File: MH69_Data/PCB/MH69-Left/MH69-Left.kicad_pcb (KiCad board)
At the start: 2 copper layers, 163.2 x 92 mm, 85 parts, among them U1 nice_nano

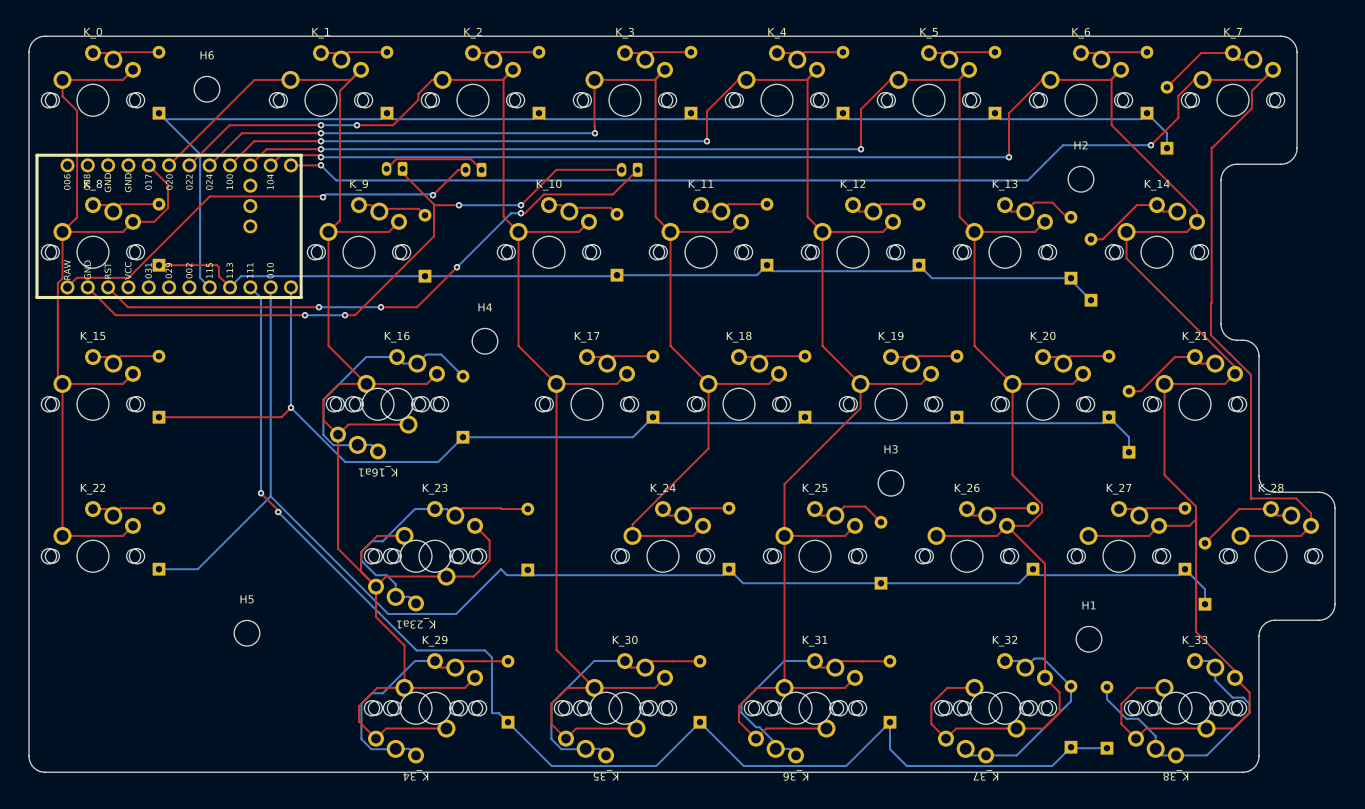
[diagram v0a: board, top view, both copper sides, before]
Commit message: Added Kailh Plated 1Us to Left
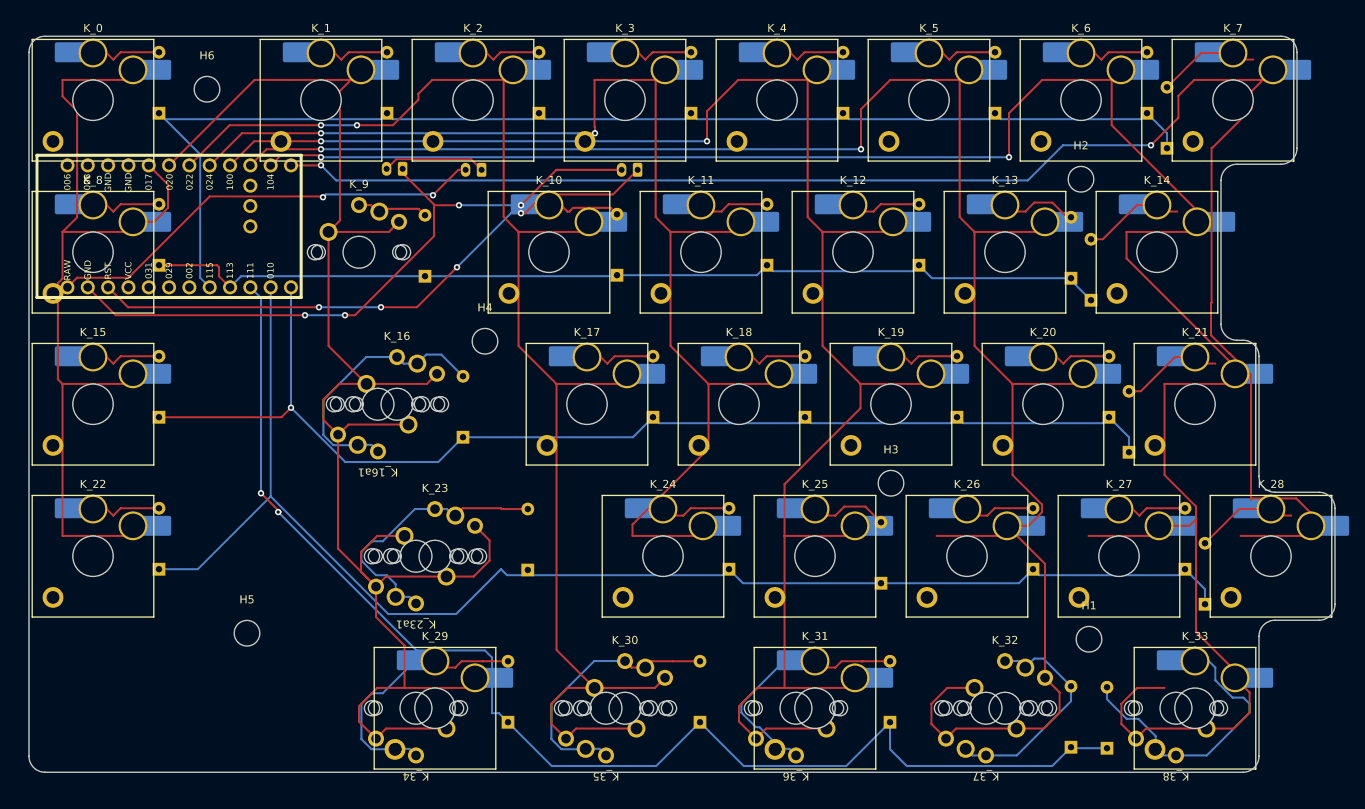
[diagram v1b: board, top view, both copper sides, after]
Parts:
- K_0, K_1, K_10, K_11, K_12, K_13, K_14, K_15, K_17, K_18, K_19, K_2, K_20, K_21, K_22, K_24, K_25, K_26, K_27, K_28, K_29, K_3, K_31, K_33, K_4, K_5, K_6, K_7, K_8: footprint cb:Choc-MX-19mm-1u -> PCM_Switch_Keyboard_Hotswap_Kailh:SW_Hotswap_Kailh_Choc_V2_Plated_1.00u

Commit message: some kicad work
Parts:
- removed K_16a1: KEYSW, cb:Choc-MX-19mm-1.75u
- K_0, K_1, K_10, K_11, K_12, K_13, K_14, K_15, K_17, K_18, K_19, K_2, K_20, K_21, K_22, K_24, K_25, K_26, K_27, K_28, K_29, K_3, K_31, K_33, K_4, K_5, K_6, K_7, K_8: footprint PCM_Switch_Keyboard_Hotswap_Kailh:SW_Hotswap_Kailh_Choc_V2_Plated_1.00u -> PCM_Switch_Keyboard_Hotswap_Kailh:SW_Hotswap_Kailh_Choc_V1_Plated_1.00u
- K_16, K_23, K_30, K_32, K_9: footprint cb:Choc-MX-19mm-1.5u -> PCM_Switch_Keyboard_Hotswap_Kailh:SW_Hotswap_Kailh_Choc_V1_Plated_1.50u
- moved K_21 7.35 mm to (170.8, 99.8)
- moved K_20 6.35 mm to (152.8, 99.8)
- moved K_22 6.18 mm to (41.8, 124.8)
- moved K_19 5.35 mm to (134.8, 99.8)
- moved K_18 4.35 mm to (116.8, 99.8)
- moved K_15 4.26 mm to (41.8, 103.8)
- moved K_17 3.35 mm to (98.8, 99.8)
- moved K_7 3.10 mm to (179.8, 61.8), turned to 180 degrees
- moved K_9 2.66 mm to (76.3, 80.8)
- moved K_14 2.60 mm to (170.8, 80.8)
- moved K_6 2.60 mm to (161.3, 61.8), turned to 180 degrees
- moved K_8 2.46 mm to (41.8, 82.8)
- moved K_16 2.10 mm to (76.3, 99.8)
- moved K_5 2.10 mm to (142.8, 61.8), turned to 180 degrees
- moved U1 2.00 mm to (51.2, 79.5)
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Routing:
- net col6: track 267.2 -> 0.00 mm, vias 2 -> 0
- net col5: track 243.8 -> 0.00 mm, vias 2 -> 0
- net col4: track 223.2 -> 0.00 mm, vias 2 -> 0
- net col7: track 209.1 -> 0.00 mm, vias 2 -> 0
- net col1: track 208.5 -> 0.00 mm
- net col2: track 176.9 -> 0.00 mm, vias 2 -> 0
- net row3: track 174.7 -> 0.00 mm
- net row4: track 162.8 -> 0.00 mm, vias 2 -> 0
- net col3: track 159.3 -> 0.00 mm, vias 2 -> 0
- net row0: track 157.0 -> 0.00 mm
- net row2: track 146.7 -> 0.00 mm, vias 1 -> 0
- net row1: track 122.0 -> 0.00 mm
- net col0: track 107.7 -> 0.00 mm
- net Net-(Batt1-Pin_1): track 84.1 -> 0.00 mm, vias 4 -> 0
- net Net-(RST1-A): track 74.3 -> 0.00 mm, vias 4 -> 0
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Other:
- board text added: "MH69-L V0"
- board text removed: "CB70S-L v3"

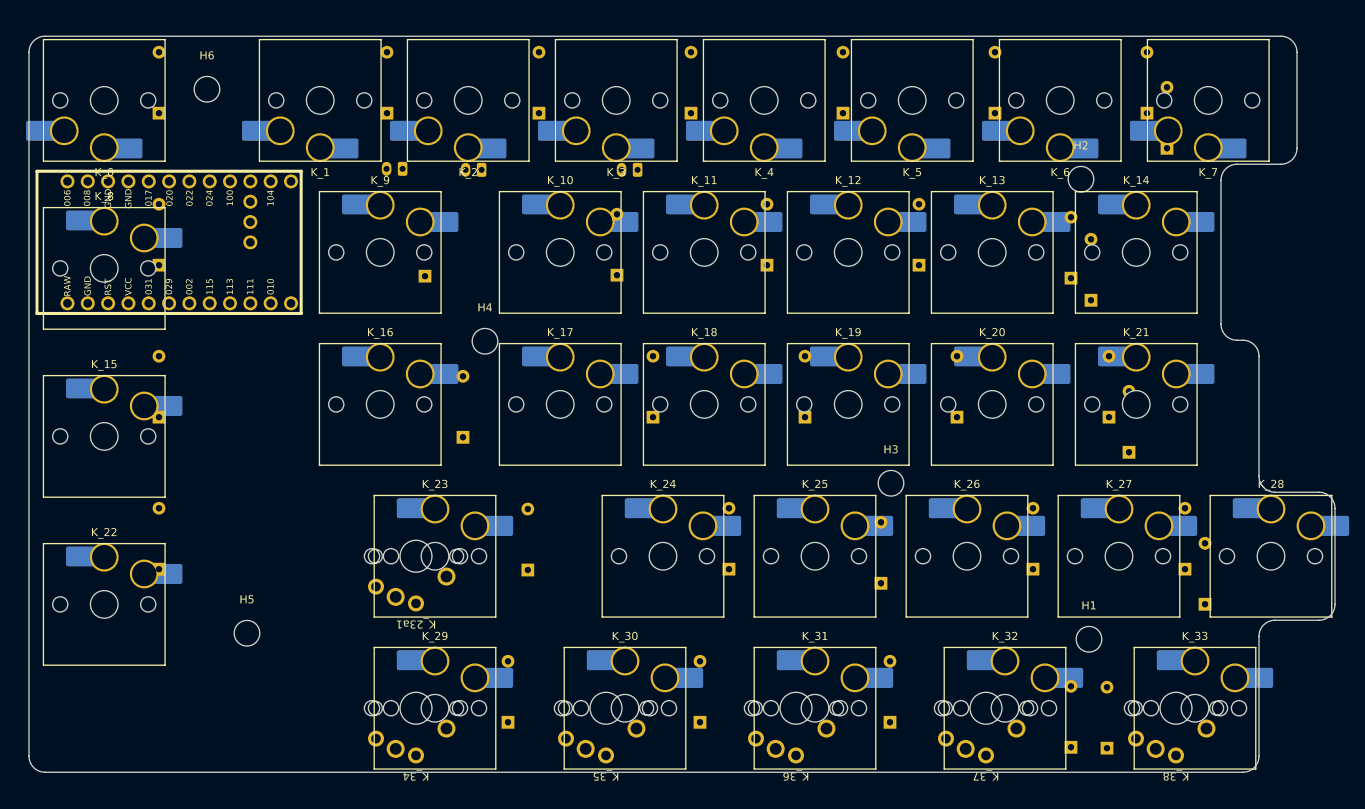
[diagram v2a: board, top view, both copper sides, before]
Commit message: Left side layout progress
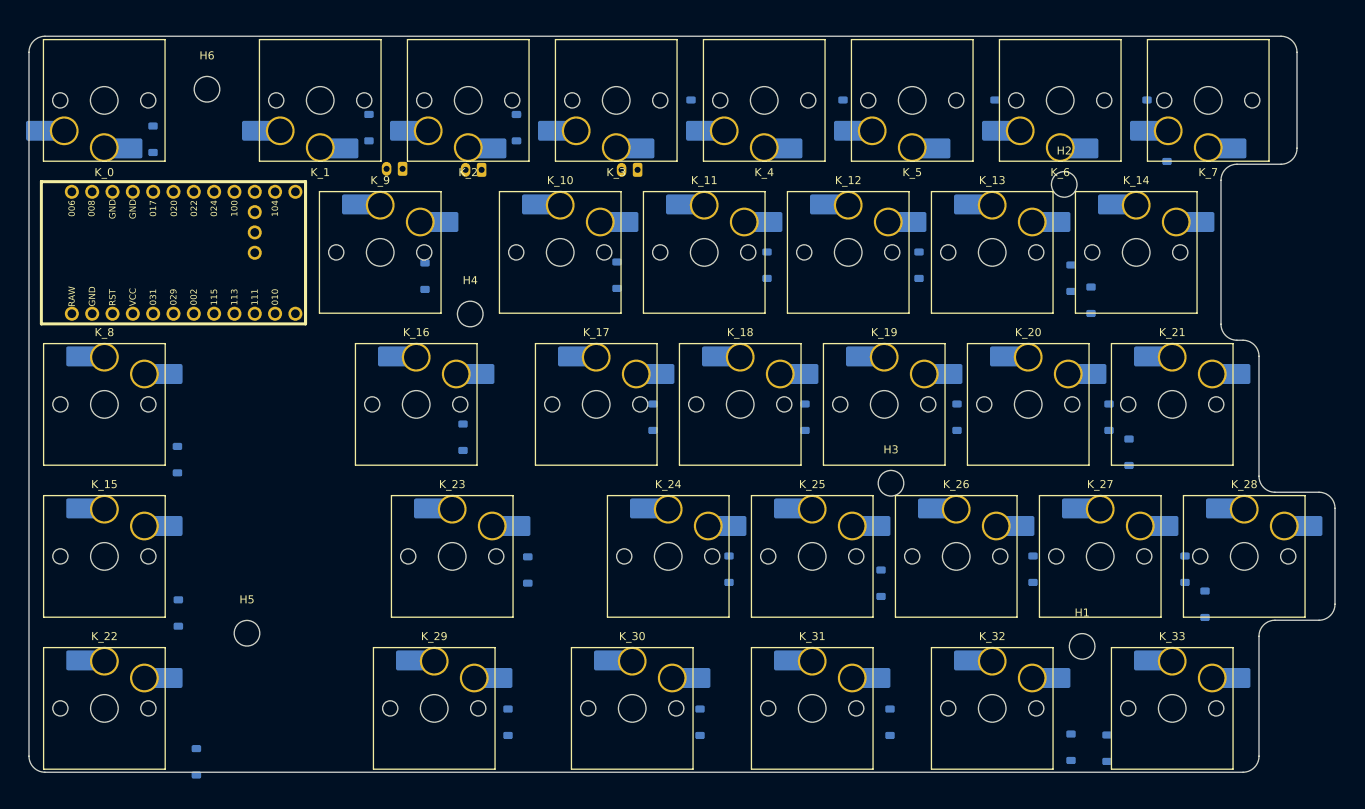
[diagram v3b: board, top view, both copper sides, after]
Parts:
- removed K_23a1: KEYSW, cb:Choc-MX-19mm-2.25u
- removed K_34, K_35, K_36, K_37, K_38: KEYSW, cb:Choc-MX-19mm-1.25u
- D_0, D_1, D_10, D_11, D_12, D_13, D_14, D_15, D_16, D_17, D_18, D_19, D_2, D_20, D_21, D_22, D_23, D_24, D_25, D_26, D_27, D_28, D_29, D_3, D_30, D_31, D_32, D_33, D_4, D_5, D_6, D_7, D_8, D_9: footprint ScottoKeebs_Components:Diode_DO-35 -> Diode_SMD:D_SOD-123
- K_29: footprint PCM_Switch_Keyboard_Hotswap_Kailh:SW_Hotswap_Kailh_Choc_V1_Plated_1.00u -> PCM_Switch_Keyboard_Hotswap_Kailh:SW_Hotswap_Kailh_Choc_V1_Plated_1.25u
- moved D_15 24.6 mm to (51.0, 125.8)
- moved D_22 24.5 mm to (53.3, 144.4)
- moved D_8 24.4 mm to (50.9, 106.7)
- moved K_8 17.0 mm to (41.8, 99.8)
- moved K_15 15.0 mm to (41.8, 118.8)
- moved K_22 13.0 mm to (41.8, 137.8)
- moved K_16 4.50 mm to (80.8, 99.8)
- moved K_17 4.50 mm to (103.3, 99.8)
- moved K_18 4.50 mm to (121.3, 99.8)
- moved K_19 4.50 mm to (139.3, 99.8)
- moved K_20 4.50 mm to (157.3, 99.8)
- moved K_21 4.50 mm to (175.3, 99.8)
- moved H4 3.87 mm to (87.5, 88.5)
- moved D_2 3.35 mm to (93.3, 65.2)
- moved K_28 3.35 mm to (184.3, 118.8)
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
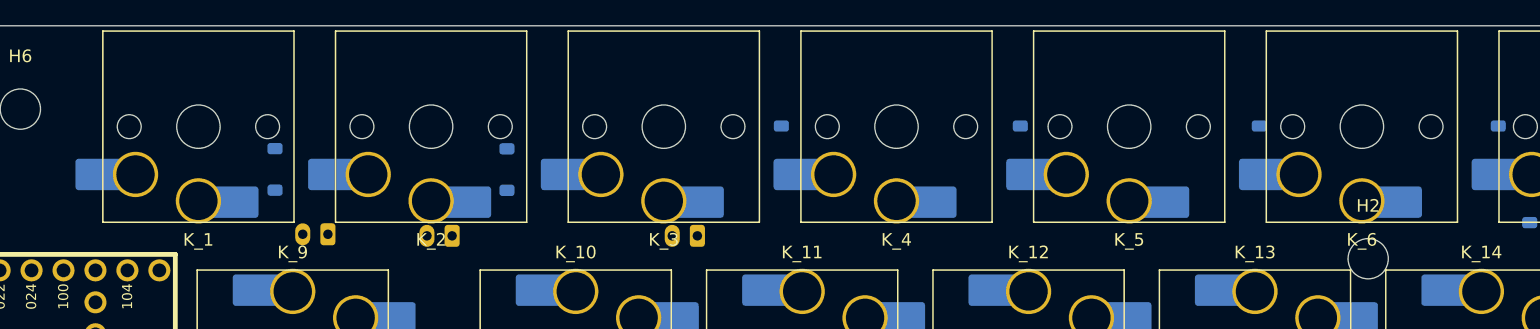
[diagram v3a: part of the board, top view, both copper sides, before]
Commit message: updated left number row
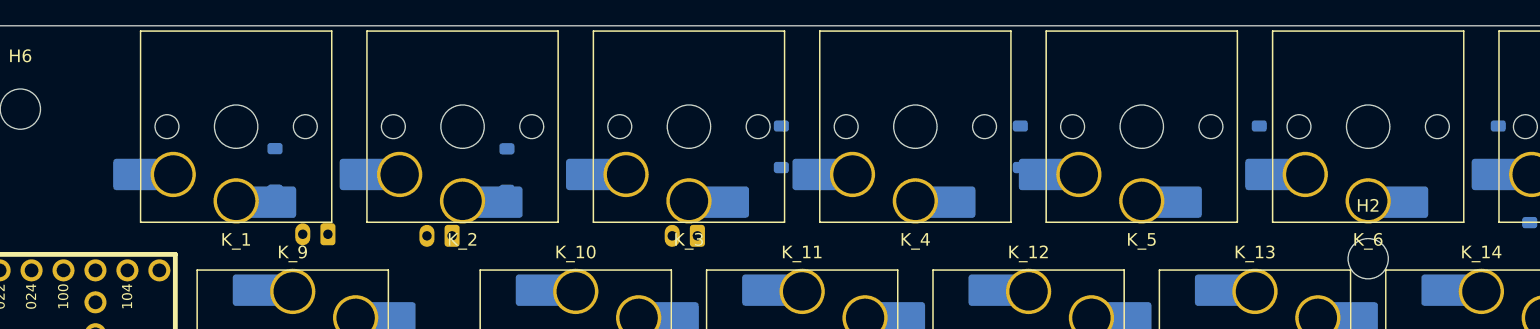
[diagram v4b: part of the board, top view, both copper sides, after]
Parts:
- moved K_1 3.00 mm to (71.8, 61.8)
- moved K_2 2.50 mm to (89.8, 61.8)
- moved K_3 2.00 mm to (107.8, 61.8)
- moved K_4 1.50 mm to (125.8, 61.8)
- moved K_5 1.00 mm to (143.8, 61.8)
- moved K_6 0.50 mm to (161.8, 61.8)
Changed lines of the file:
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@@
 	(footprint "PCM_Switch_Keyboard_Hotswap_Kailh:SW_Hotswap_Kailh_Choc_V1_Plated_1.00u"
 		(layer "F.Cu")
-		(at 105.78 61.77 180)
+		(at 107.78 61.77 180)
 		(descr "Kailh Choc keyswitch V1 CPG1350 V1 Hotswap Plated Keycap 1.00u")
 		(tags "Kailh Choc Keyswitch Switch CPG1350 V1 Hotswap Plated Cutout Keycap 1.00u")
@@
 	(footprint "PCM_Switch_Keyboard_Hotswap_Kailh:SW_Hotswap_Kailh_Choc_V1_Plated_1.00u"
 		(layer "F.Cu")
-		(at 87.28 61.77 180)
+		(at 89.78 61.77 180)
 		(descr "Kailh Choc keyswitch V1 CPG1350 V1 Hotswap Plated Keycap 1.00u")
 		(tags "Kailh Choc Keyswitch Switch CPG1350 V1 Hotswap Plated Cutout Keycap 1.00u")
@@
 	(footprint "PCM_Switch_Keyboard_Hotswap_Kailh:SW_Hotswap_Kailh_Choc_V1_Plated_1.00u"
 		(layer "F.Cu")
-		(at 68.78 61.77 180)
+		(at 71.78 61.77 180)
 		(descr "Kailh Choc keyswitch V1 CPG1350 V1 Hotswap Plated Keycap 1.00u")
 		(tags "Kailh Choc Keyswitch Switch CPG1350 V1 Hotswap Plated Cutout Keycap 1.00u")
@@
 	(footprint "PCM_Switch_Keyboard_Hotswap_Kailh:SW_Hotswap_Kailh_Choc_V1_Plated_1.00u"
 		(layer "F.Cu")
-		(at 161.28 61.77 180)
+		(at 161.78 61.77 180)
 		(descr "Kailh Choc keyswitch V1 CPG1350 V1 Hotswap Plated Keycap 1.00u")
 		(tags "Kailh Choc Keyswitch Switch CPG1350 V1 Hotswap Plated Cutout Keycap 1.00u")
@@
 	(footprint "PCM_Switch_Keyboard_Hotswap_Kailh:SW_Hotswap_Kailh_Choc_V1_Plated_1.00u"
 		(layer "F.Cu")
-		(at 142.78 61.77 180)
+		(at 143.78 61.77 180)
 		(descr "Kailh Choc keyswitch V1 CPG1350 V1 Hotswap Plated Keycap 1.00u")
 		(tags "Kailh Choc Keyswitch Switch CPG1350 V1 Hotswap Plated Cutout Keycap 1.00u")
@@
 	(footprint "PCM_Switch_Keyboard_Hotswap_Kailh:SW_Hotswap_Kailh_Choc_V1_Plated_1.00u"
 		(layer "F.Cu")
-		(at 124.28 61.77 180)
+		(at 125.78 61.77 180)
 		(descr "Kailh Choc keyswitch V1 CPG1350 V1 Hotswap Plated Keycap 1.00u")
 		(tags "Kailh Choc Keyswitch Switch CPG1350 V1 Hotswap Plated Cutout Keycap 1.00u")

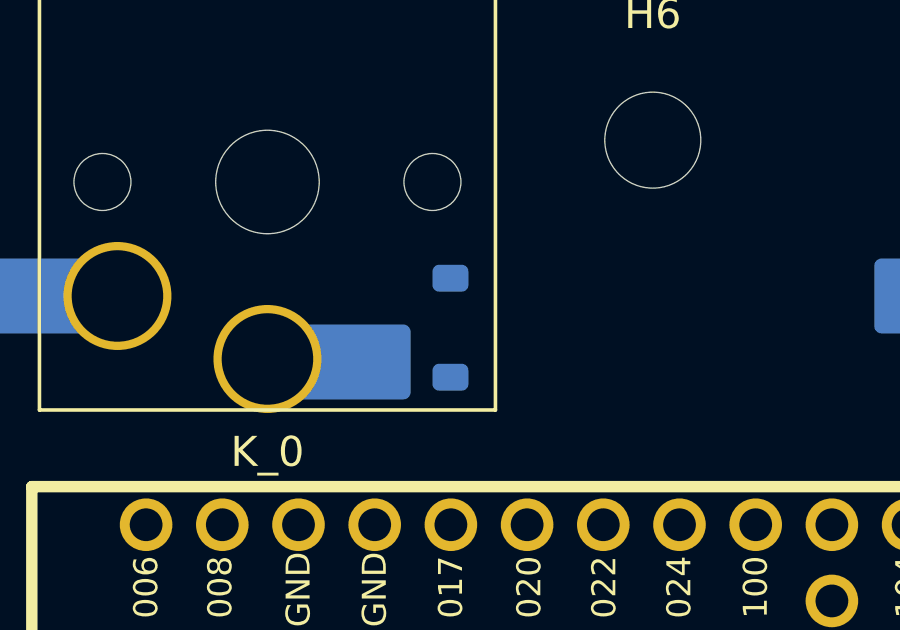
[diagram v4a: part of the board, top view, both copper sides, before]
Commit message: tiny change to a single diode
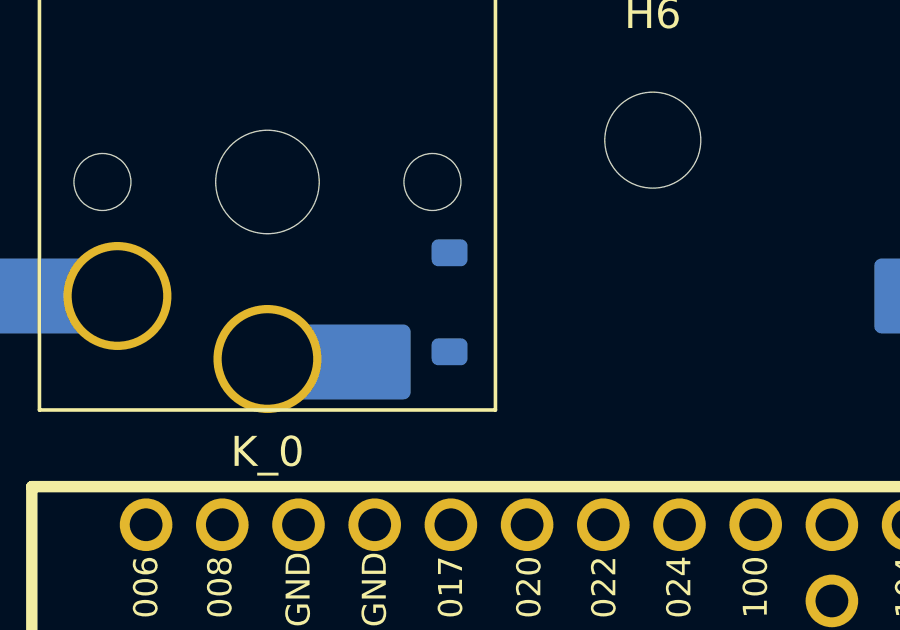
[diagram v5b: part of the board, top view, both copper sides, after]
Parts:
- moved D_0 0.85 mm to (47.9, 65.8)
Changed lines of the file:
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@@
 	(footprint "Diode_SMD:D_SOD-123"
 		(layer "B.Cu")
-		(at 47.88 66.6275 90)
+		(at 47.85 65.78 90)
 		(descr "SOD-123")
 		(tags "SOD-123")

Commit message: very minor layout tweaking
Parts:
- turned K_0 to 0 degrees
- turned K_1 to 0 degrees
- turned K_2 to 0 degrees
- turned K_3 to 0 degrees
- turned K_4 to 0 degrees
- turned K_5 to 0 degrees
- turned K_6 to 0 degrees
- turned K_7 to 0 degrees
